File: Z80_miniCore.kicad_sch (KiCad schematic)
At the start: 37 parts, among them J1 ICSP, J2 UART, J3 I2C, J5 MicroSD, J7 USB_B_Mini, SW1 ON|OFF, SW2 Z80_RESET, U1 Z84C00/PLCC, U2 PIC1-MMU, U3 AS6C4008-55PCN, U4 SST39SF010, U5 PIC2-LOADER, Y1 CANNED-DIP8, Y2 Crystal

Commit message: change ROM/footprint -> PLCC32
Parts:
- U4: footprint Package_DIP:DIP-32_W15.24mm -> Package_LCC:PLCC-32_THT-Socket
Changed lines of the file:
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@@
 			)
 		)
-		(property "Footprint" "Package_DIP:DIP-32_W15.24mm"
+		(property "Footprint" "Package_LCC:PLCC-32_THT-Socket"
 			(at 165.1 50.8 0)
 			(hide yes)

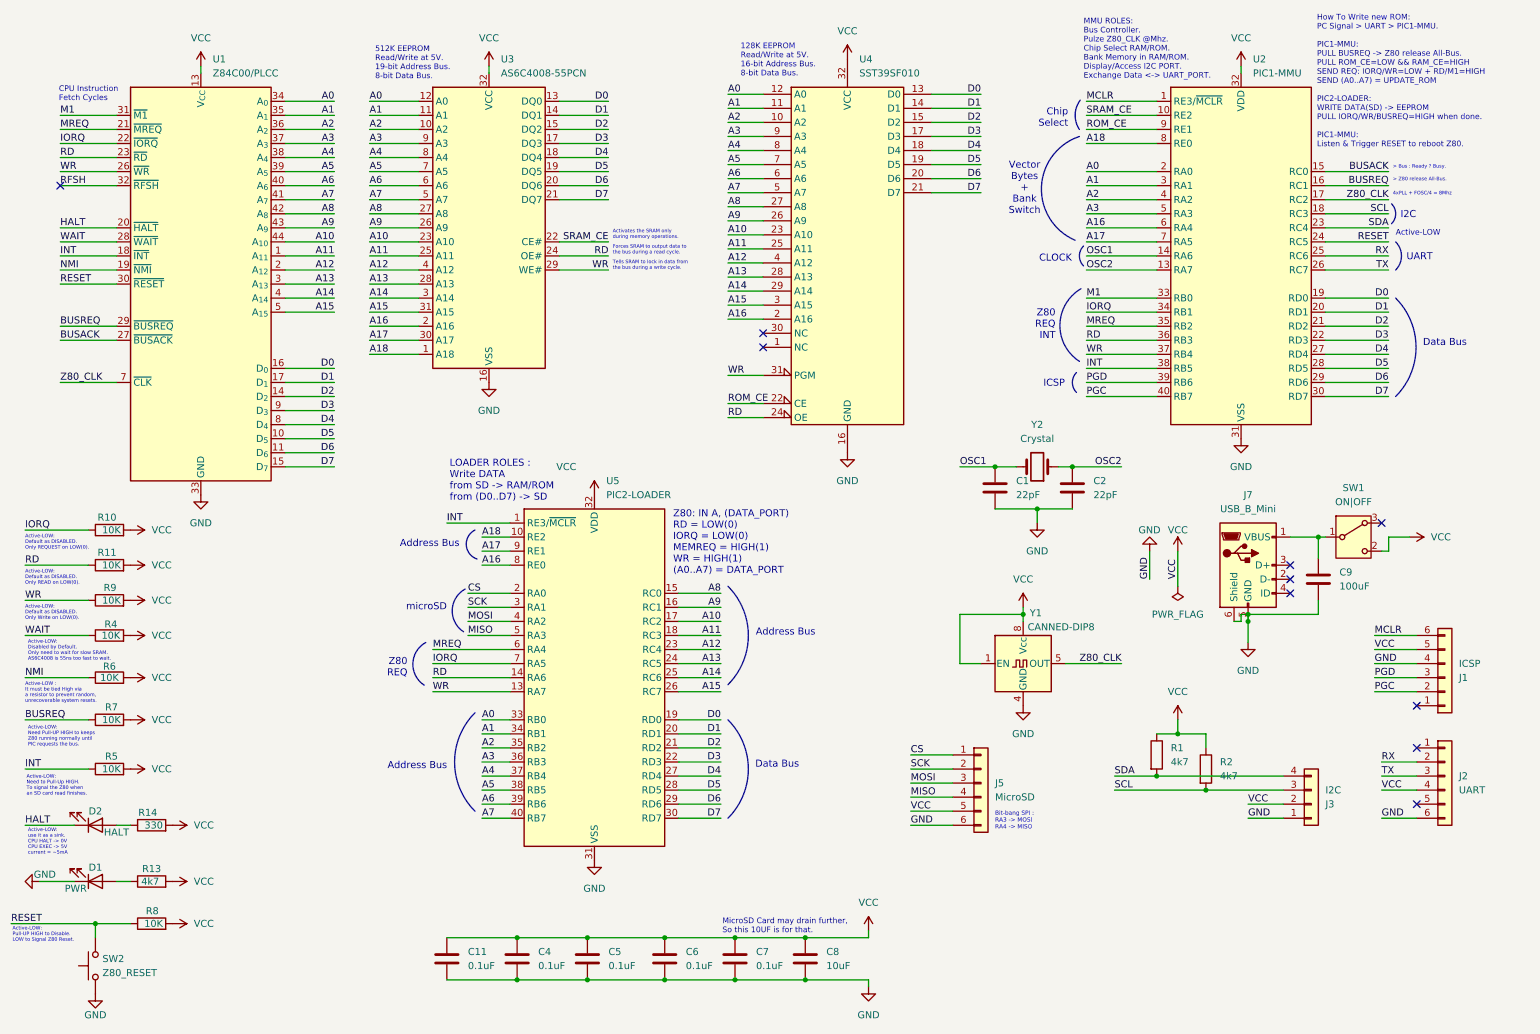
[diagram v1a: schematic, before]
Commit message: Add MMU for ROM:Fixed 16K + Swappable 16K + RAM:32K setup.
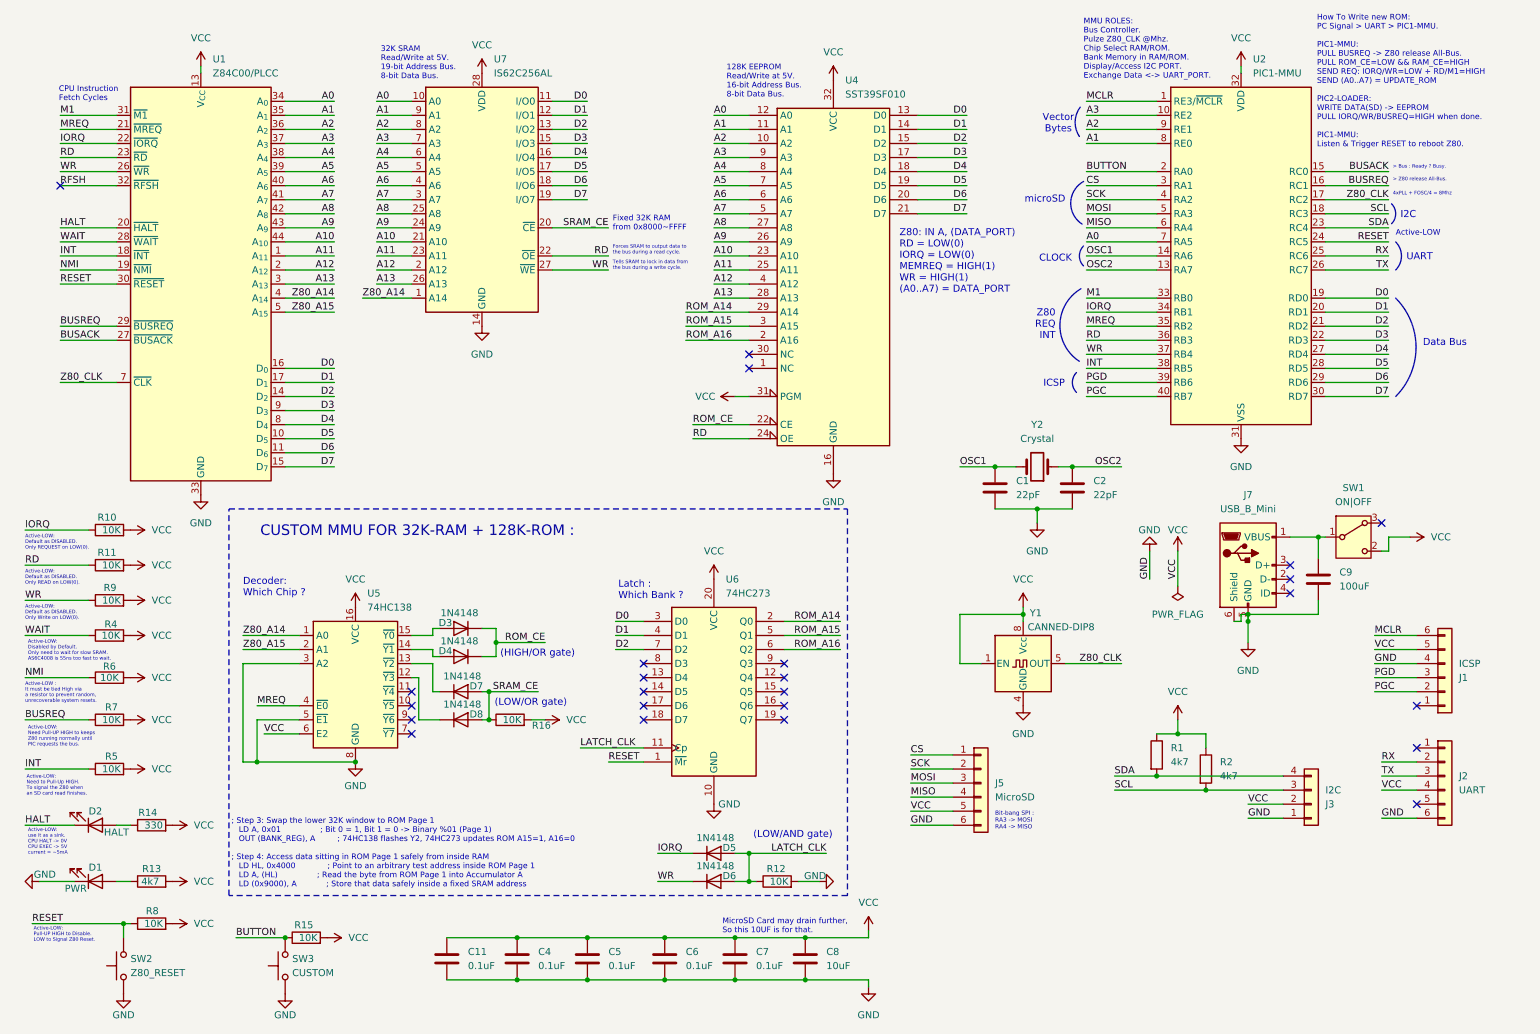
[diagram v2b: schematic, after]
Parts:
- removed U3: AS6C4008-55PCN, Package_DIP:DIP-32_W15.24mm, symbol Memory_RAM:AS6C4008-55PCN
- removed U5: PIC2-LOADER, Package_DIP:DIP-40_W15.24mm, symbol MCU_Microchip_PIC18:PIC18F4520-xP
- added D3, D4, D5, D6, D7, D8: 1N4148, Diode_THT:D_A-405_P10.16mm_Horizontal, symbol Device:D
- added R12, R15, R16: 10K, Resistor_THT:R_Axial_DIN0207_L6.3mm_D2.5mm_P10.16mm_Horizontal, symbol Device:R
- added SW3: CUSTOM, Button_Switch_THT:SW_PUSH_6mm, symbol Switch:SW_Push
- added U5: 74HC138, symbol 74xx:74HC138
- added U6: 74HC273, symbol 74xx:74HC273
- added U7: IS62C256AL, Package_SO:SOP-28_8.4x18.16mm_P1.27mm, symbol Memory_RAM:IS62C256AL
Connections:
- net A17 is gone; now on net A0: U2.7 (RA5)
- net A18 is gone; now on net A1: U2.8 (RE0)
- net A0: now also U7.10 (A0); no longer U2.2 (RA0)
- net A1: now also U7.9 (A1); no longer U2.3 (RA1)
- net A10: now also U7.21 (A10)
- net A11: now also U7.23 (A11)
- net A12: now also U7.2 (A12)
- net A13: now also U7.26 (A13)
- net A2: now also U2.9 (RE1), U7.8 (A2); no longer U2.4 (RA2)
- net A3: now also U2.10 (RE2), U7.7 (A3); no longer U2.5 (RA3)
- net A4: now also U7.6 (A4)
- net A5: now also U7.5 (A5)
- net A6: now also U7.4 (A6)
- net A7: now also U7.3 (A7)
- net A8: now also U7.25 (A8)
- net A9: now also U7.24 (A9)
- net CS: now also U2.3 (RA1)
- net D0: now also U6.3 (D0), U7.11 (I/O0)
- net D1: now also U6.4 (D1), U7.12 (I/O1)
- net D2: now also U6.7 (D2), U7.13 (I/O2)
- net D3: now also U7.15 (I/O3)
- net D4: now also U7.16 (I/O4)
- net D5: now also U7.17 (I/O5)
- net D6: now also U7.18 (I/O6)
- net D7: now also U7.19 (I/O7)
- net GND: now also R12.2, SW3.1, U5.3 (A2), U5.5 (~{E1}), U5.8 (GND), U6.10 (GND), U7.14 (GND)
- net IORQ: now also D5.1 (K)
- net MISO: now also U2.6 (RA4)
- net MOSI: now also U2.5 (RA3)
- net MREQ: now also U5.4 (~{E0})
- net RD: now also U7.22 (~{OE})
- net RESET: now also U6.1 (~{Mr})
- net ROM_CE: now also D3.1 (K), D4.1 (K); no longer U2.9 (RE1)
- net SCK: now also U2.4 (RA2)
- net SRAM_CE: now also D7.2 (A), D8.2 (A), R16.1, U7.20 (~{CE}); no longer U2.10 (RE2)
- net VCC: now also U4.31 (PGM), R15.2, R16.2, U5.16 (VCC), U5.6 (E2), U6.20 (VCC), U7.28 (VDD)
- net WR: now also D6.1 (K), U7.27 (~{WE}); no longer U4.31 (PGM)
- net A14 renamed ROM_A14
- net ROM_A14: now also U6.2 (Q0); no longer U1.4 (A_{14})
- net A15 renamed ROM_A15
- net ROM_A15: now also U6.5 (Q1); no longer U1.5 (A_{15})
- net A16 renamed ROM_A16
- net ROM_A16: now also U6.6 (Q2); no longer U2.6 (RA4)
- new net: D7.1 (K), U5.13 (~{Y2})
- new net: D8.1 (K), U5.12 (~{Y3})
- new net: D3.2 (A), U5.15 (~{Y0})
- new net: D4.2 (A), U5.14 (~{Y1})
- new net BUTTON: R15.1, SW3.2, U2.2 (RA0)
- new net LATCH_CLK: D5.2 (A), D6.2 (A), R12.1, U6.11 (Cp)
- new net Z80_A14: U1.4 (A_{14}), U5.1 (A0), U7.1 (A14)
- new net Z80_A15: U1.5 (A_{15}), U5.2 (A1)
- no-connect marks 10 -> 24
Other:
- note added: "(HIGH/OR gate)"
- note added: "(LOW/AND gate)"
- note added: "(LOW/OR gate)"
- note added: "32K SRAM Read/Write at 5V. 19-bit Address Bus. 8-bit Data Bus."
- note added: "; Step 3: Swap the lower 32K window to ROM Page 1 LD A, 0x01 ; Bit 0 = 1, Bit 1 = 0 -> Binary %01 (Page 1) OUT (BANK_REG), A ; 74HC138 flashes Y2, 74HC273 updates ROM A15=1, A16=0 ; Step 4: Access data sitting in ROM Page 1 safely from inside RAM LD HL, 0x4000 ; Point to an arbitrary test address inside ROM Page 1 LD A, (HL) ; Read the byte from ROM Page 1 into Accumulator A LD (0x9000), A ; Stor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"
- note added: "CUSTOM MMU FOR 32K-RAM + 128K-ROM :"
- note added: "Decoder: Which Chip ?"
- note added: "Fixed 32K RAM from 0x8000~FFFF"
- note added: "Latch : Which Bank ?"
- note added: "Vector Bytes"
- note removed: "512K EEPROM Read/Write at 5V. 19-bit Address Bus. 8-bit Data Bus."
- note removed: "Activates the SRAM only during memory operations."
- note removed: "Address Bus"
- note removed: "Chip Select"
- note removed: "LOADER ROLES : Write DATA from SD -> RAM/ROM from (D0..D7) -> SD"
- note removed: "Vector Bytes + Bank Switch"
- note removed: "Z80 REQ"
- moved on the sheet: SW2, U4

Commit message: Replace ROM + MMU/74HC138.
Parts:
- removed D3, D4, D5, D6, D7, D8: 1N4148, Diode_THT:D_A-405_P10.16mm_Horizontal, symbol Device:D
- removed R16: 10K, Resistor_THT:R_Axial_DIN0207_L6.3mm_D2.5mm_P10.16mm_Horizontal, symbol Device:R
- removed U4: SST39SF010, Package_LCC:PLCC-32_THT-Socket, symbol Memory_Flash:SST39SF010
- removed U5: 74HC138, symbol 74xx:74HC138
- removed U6: 74HC273, symbol 74xx:74HC273
- added U3: 28C256, Package_DIP:DIP-28_W15.24mm, symbol Memory_EEPROM:28C256
- added U4: 74HC138, Package_DIP:DIP-16_W7.62mm, symbol 74xx:74HC138
- U7: footprint Package_SO:SOP-28_8.4x18.16mm_P1.27mm -> Package_DIP:DIP-28_W15.24mm
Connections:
- net LATCH_CLK is gone; now on net MREQ: R12.1
- net A0: now also U3.10 (A0)
- net A1: now also U3.9 (A1)
- net A10: now also U3.21 (A10)
- net A11: now also U3.23 (A11)
- net A12: now also U3.2 (A12)
- net A13: now also U3.26 (A13)
- net A2: now also U3.8 (A2)
- net A3: now also U3.7 (A3)
- net A4: now also U3.6 (A4)
- net A5: now also U3.5 (A5)
- net A6: now also U3.4 (A6)
- net A7: now also U3.3 (A7)
- net A8: now also U3.25 (A8)
- net A9: now also U3.24 (A9)
- net D0: now also U3.11 (D0)
- net D1: now also U3.12 (D1)
- net D2: now also U3.13 (D2)
- net D3: now also U3.15 (D3)
- net D4: now also U3.16 (D4)
- net D5: now also U3.17 (D5)
- net D6: now also U3.18 (D6)
- net D7: now also U3.19 (D7)
- net GND: now also U3.14 (GND), U4.2 (A1), U4.3 (A2), U4.8 (GND); no longer R12.2
- net MREQ: now also U4.4 (~{E0})
- net RD: now also U3.22 (~{OE})
- net RFSH: now also U4.5 (~{E1})
- net ROM_CE: now also U3.20 (~{CS}), U4.15 (~{Y0})
- net SRAM_CE: now also U4.14 (~{Y1})
- net VCC: now also R12.2, U3.28 (VCC), U4.16 (VCC), U4.6 (E2)
- net WR: now also U3.27 (~{WE})
- net Z80_A15: now also U4.1 (A0)
- net Z80_A14 renamed A14
- net A14: now also U3.1 (A14)
- no-connect marks 24 -> 13
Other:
- note added: "32K EEPROM Read/Write at 5V. 16-bit Address Bus. 8-bit Data Bus."
- note added: "CUSTOM MMU FOR 32K-RAM + 32K-ROM :"
- note added: "ORG $0000 ;Start with Rom at 0x0000 LD A, (ROM_DATA) ;Load Rom data -> register A LD ($8000), A ;Write to Ram @ 0x8000 LD B, ($8000) ;Read back from Ram ORG $0050 ROM_DATA: DB $42 ;Test Byte in ROM."
- note removed: "(HIGH/OR gate)"
- note removed: "(LOW/AND gate)"
- note removed: "(LOW/OR gate)"
- note removed: "128K EEPROM Read/Write at 5V. 16-bit Address Bus. 8-bit Data Bus."
- note removed: "; Step 3: Swap the lower 32K window to ROM Page 1 LD A, 0x01 ; Bit 0 = 1, Bit 1 = 0 -> Binary %01 (Page 1) OUT (BANK_REG), A ; 74HC138 flashes Y2, 74HC273 updates ROM A15=1, A16=0 ; Step 4: Access data sitting in ROM Page 1 safely from inside RAM LD HL, 0x4000 ; Point to an arbitrary test address inside ROM Page 1 LD A, (HL) ; Read the byte from ROM Page 1 into Accumulator A LD (0x9000), A ; Stor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"
- note removed: "CUSTOM MMU FOR 32K-RAM + 128K-ROM :"
- note removed: "Decoder: Which Chip ?"
- note removed: "Latch : Which Bank ?"
- moved on the sheet: R10, R11, R4, R6, R7, R9, U1, U7
